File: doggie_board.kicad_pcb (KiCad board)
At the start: 4 copper layers, 117.6 x 127 mm, 110 parts, among them J1 Conn_01x03, J2 XT90PW-M, J3 XT90PW-M, J4 Conn_01x02, J5 Conn_01x03, J5V1 48v, J5V10 48v, J5V11 48v, J5V12 48v, J5V13 12v, J5V14 12v, J5V15 12v, J5V16 12v, J5V17 3.3v, J5V18 3.3v, J5V19 3.3v, J5V2 48v, J5V20 3.3v, J5V21 5v, J5V22 5v, J5V23 5v, J5V24 5v, J5V3 48v, J5V4 48v, J5V5 48v, J5V6 48v, J5V7 48v, J5V8 48v, J5V9 48v, J6 Conn_01x02, J7 Conn_01x03, J8 Conn_01x03, Q1 PSMN3R7-100BSEJ, Q10 2N7002, Q11 2N7002, Q12 2N7002, Q2 PSMN3R7-100BSEJ, Q3 PSMN3R7-100BSEJ, Q4 PSMN3R7-100BSEJ, Q5 PSMN3R7-100BSEJ, Q6 PSMN3R7-100BSEJ, Q7 Q_NMOS, Q8 Q_NMOS, Q9 2N7002, U1 TPS2490, U2 LM5148RGYR, U3 TPS566242DRLR, U4 TPS566242DRLR

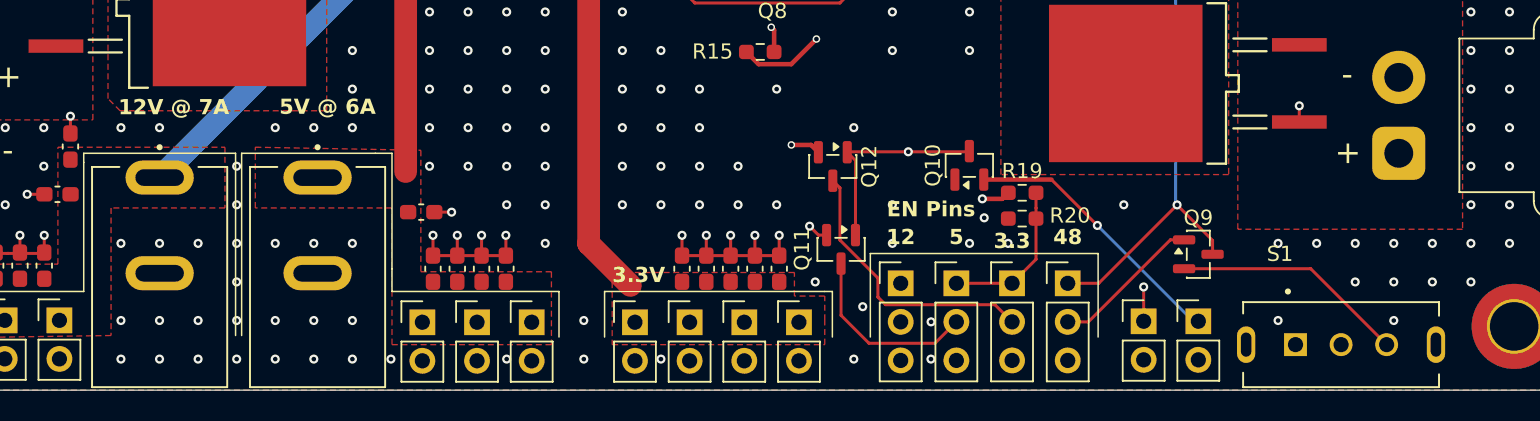
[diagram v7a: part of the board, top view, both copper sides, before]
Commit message: added header labels
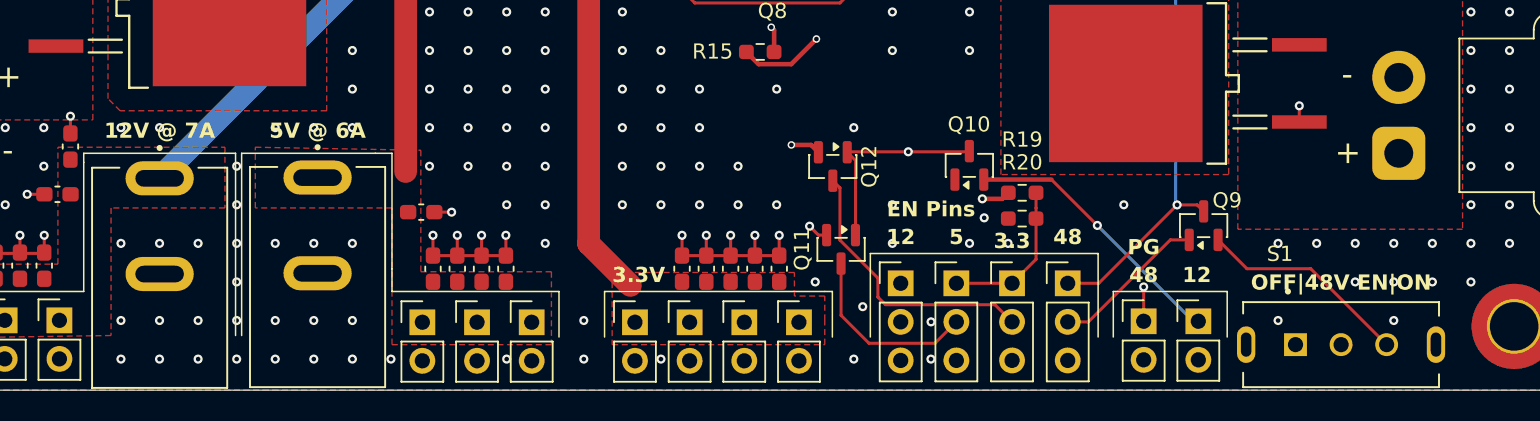
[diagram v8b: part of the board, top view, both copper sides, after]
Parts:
- moved Q9 1.92 mm to (132.6, 154.8), turned to 90 degrees
- moved J5V13 0.05 mm to (63.8, 151.7)
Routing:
- net /High Side Power Switch/sw_low: track 98.7 -> 96.4 mm
- net Net-(Q9-S): track 15.4 -> 14.0 mm
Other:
- board text added: "OFF|48V EN|ON"
- board text added: "PG"
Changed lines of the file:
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@@
 		(tags "resistor handsolder")
 		(property "Reference" "R20"
-			(at -3.15 0.2 180)
+			(at 0 3.7 180)
 			(layer "F.SilkS")
 			(effects
@@
 		(placed yes)
 		(layer "F.Cu")
-		(at 132.2 156.65)
+		(at 132.55 154.7625 90)
 		(descr "SOT, 3 Pin (JEDEC TO-236 Var AB https://www.jedec.org/document_search?search_api_views_fulltext=TO-236), generated with kicad-footprint-generator ipc_gullwing_generator.py")
 		(tags "SOT TO_SOT_SMD")
 		(property "Reference" "Q9"
-			(at 0 -2.4 0)
+			(at 1.6625 1.55 0)
 			(layer "F.SilkS")
 			(effects
@@
 		)
 		(property "Value" "2N7002"
-			(at 0 2.4 0)
+			(at 0 2.4 90)
 			(layer "F.Fab")
 			(effects
@@
 		)
 		(property "Datasheet" "https://www.onsemi.com/pub/Collateral/NDS7002A-D.PDF"
-			(at 0 0 0)
+			(at 0 0 90)
 			(layer "F.Fab")
 			(hide yes)
@@
 		)
 		(property "Description" "0.115A Id, 60V Vds, N-Channel MOSFET, SOT-23"
-			(at 0 0 0)
+			(at 0 0 90)
 			(layer "F.Fab")
 			(hide yes)
@@
 		(attr smd)
 		(fp_line
-			(start -0.76 -1.56)
-			(end 0.76 -1.56)
+			(start 0.76 -1.56)
+			(end 0.76 -0.56)
 			(stroke
 				(width 0.12)
@@
 		)
 		(fp_line
-			(start -0.76 -1.51)
-			(end -0.76 -1.56)
+			(start -0.76 -1.56)
+			(end 0.76 -1.56)
 			(stroke
 				(width 0.12)
@@
 		)
 		(fp_line
-			(start -0.76 0.39)
-			(end -0.76 -0.39)
+			(start -0.76 -1.51)
+			(end -0.76 -1.56)
 			(stroke
 				(width 0.12)
@@
 		)
 		(fp_line
-			(start -0.76 1.56)
-			(end -0.76 1.51)
+			(start -0.76 0.39)
+			(end -0.76 -0.39)
 			(stroke
 				(width 0.12)
@@
 		)
 		(fp_line
-			(start 0.76 -1.56)
-			(end 0.76 -0.56)
+			(start 0.76 0.56)
+			(end 0.76 1.56)
 			(stroke
 				(width 0.12)
@@
 		)
 		(fp_line
-			(start 0.76 0.56)
-			(end 0.76 1.56)
+			(start 0.76 1.56)
+			(end -0.76 1.56)
 			(stroke
 				(width 0.12)
@@
 		)
 		(fp_line
-			(start 0.76 1.56)
-			(end -0.76 1.56)
+			(start -0.76 1.56)
+			(end -0.76 1.51)
 			(stroke
 				(width 0.12)
@@
 		)
 		(fp_line
-			(start -1.93 -1.5)
-			(end -0.9 -1.5)
+			(start 0.9 -1.7)
+			(end 0.9 -0.55)
 			(stroke
 				(width 0.05)
@@
 		)
 		(fp_line
-			(start -1.93 -0.39)
-			(end -1.93 -1.5)
+			(start -0.9 -1.7)
+			(end 0.9 -1.7)
 			(stroke
 				(width 0.05)
@@
 		)
 		(fp_line
-			(start -1.93 0.39)
-			(end -0.9 0.39)
+			(start -0.9 -1.5)
+			(end -0.9 -1.7)
 			(stroke
 				(width 0.05)
@@
 		)
 		(fp_line
-			(start -1.93 1.5)
-			(end -1.93 0.39)
+			(start -1.93 -1.5)
+			(end -0.9 -1.5)
 			(stroke
 				(width 0.05)
@@
 		)
 		(fp_line
-			(start -0.9 -1.7)
-			(end 0.9 -1.7)
+			(start 1.93 -0.55)
+			(end 1.93 0.55)
 			(stroke
 				(width 0.05)
@@
 		)
 		(fp_line
-			(start -0.9 -1.5)
-			(end -0.9 -1.7)
+			(start 0.9 -0.55)
+			(end 1.93 -0.55)
 			(stroke
 				(width 0.05)
@@
 		)
 		(fp_line
-			(start -0.9 0.39)
-			(end -0.9 -0.39)
+			(start -1.93 -0.39)
+			(end -1.93 -1.5)
 			(stroke
 				(width 0.05)
@@
 		)
 		(fp_line
-			(start -0.9 1.5)
-			(end -1.93 1.5)
+			(start -0.9 0.39)
+			(end -0.9 -0.39)
 			(stroke
 				(width 0.05)
@@
 		)
 		(fp_line
-			(start -0.9 1.7)
-			(end -0.9 1.5)
+			(start -1.93 0.39)
+			(end -0.9 0.39)
 			(stroke
 				(width 0.05)
@@
 		)
 		(fp_line
-			(start 0.9 -1.7)
-			(end 0.9 -0.55)
+			(start 1.93 0.55)
+			(end 0.9 0.55)
 			(stroke
 				(width 0.05)
@@
 		)
 		(fp_line
-			(start 0.9 -0.55)
-			(end 1.93 -0.55)
+			(start 0.9 0.55)
+			(end 0.9 1.7)
 			(stroke
 				(width 0.05)
@@
 		)
 		(fp_line
-			(start 0.9 0.55)
-			(end 0.9 1.7)
+			(start -0.9 1.5)
+			(end -1.93 1.5)
 			(stroke
 				(width 0.05)
@@
 		)
 		(fp_line
-			(start 0.9 1.7)
-			(end -0.9 1.7)
+			(start -1.93 1.5)
+			(end -1.93 0.39)
 			(stroke
 				(width 0.05)
@@
 		)
 		(fp_line
-			(start 1.93 -0.55)
-			(end 1.93 0.55)
+			(start 0.9 1.7)
+			(end -0.9 1.7)
 			(stroke
 				(width 0.05)
@@
 		)
 		(fp_line
-			(start 1.93 0.55)
-			(end 0.9 0.55)
+			(start -0.9 1.7)
+			(end -0.9 1.5)
 			(stroke
 				(width 0.05)
@@
 		)
 		(fp_text user "${REFERENCE}"
-			(at 0 0 90)
+			(at 0 0 0)
 			(layer "F.Fab")
 			(effects
@@
 		)
 		(pad "1" smd roundrect
-			(at -0.9375 -0.95)
+			(at -0.9375 -0.95 90)
 			(size 1.475 0.6)
 			(layers "F.Cu" "F.Mask" "F.Paste")
@@
 		)
 		(pad "2" smd roundrect
-			(at -0.9375 0.95)
+			(at -0.9375 0.95 90)
 			(size 1.475 0.6)
 			(layers "F.Cu" "F.Mask" "F.Paste")
@@
 		)
 		(pad "3" smd roundrect
-			(at 0.9375 0)
+			(at 0.9375 0 90)
 			(size 1.475 0.6)
 			(layers "F.Cu" "F.Mask" "F.Paste")
@@
 		(tags "resistor handsolder")
 		(property "Reference" "R19"
-			(at 0 -1.43 0)
+			(at 0 -3.5 0)
 			(layer "F.SilkS")
 			(effects
@@
 	(footprint "footprints:CUI_PJ-037A"
 		(layer "F.Cu")
-		(at 63.8 151.6 -90)
+		(at 63.8 151.65 -90)
 		(property "Reference" "J5V13"
 			(at 2.485784 -6.76712 90)
@@
 		(tags "SOT TO_SOT_SMD")
 		(property "Reference" "Q10"
-			(at 0 -2.4 90)
+			(at 2.6941 -0.0208 0)
 			(layer "F.SilkS")
 			(effects
@@
 	)
 	(gr_line
+		(start 126.6 162.1)
+		(end 126.6 159.1)
+		(stroke
+			(width 0.1)
+			(type default)
+		)
+		(layer "F.SilkS")
+	)
+	(gr_line
 		(start 58.8 150)
 		(end 68.8 150)
@@
 	)
 	(gr_line
+		(start 134.1 159.1)
+		(end 134.1 162.1)
+		(stroke
+			(width 0.1)
+			(type default)
+		)
+		(layer "F.SilkS")
+	)
+	(gr_line
 		(start 74.3 50.2)
 		(end 74.2 54.6)
@@
 	)
 	(gr_line
+		(start 126.6 159.1)
+		(end 134.1 159.1)
+		(stroke
+			(width 0.1)
+			(type default)
+		)
+		(layer "F.SilkS")
+	)
+	(gr_line
 		(start 78 150)
 		(end 79.1 150)
@@
 		(layer "Edge.Cuts")
 	)
-	(gr_text "12V @ 7A\n"
-		(at 61.075 147.55 0)
+	(gr_text "12V @ 7A \n"
+		(at 63.8 149.1 0)
 		(layer "F.SilkS")
 		(effects
@@
 				(bold yes)
 			)
-			(justify left bottom)
+			(justify bottom)
 		)
 	)
@@
 	)
 	(gr_text "5V @ 6A"
-		(at 71.675 147.525 0)
+		(at 74.2 149.1 0)
 		(layer "F.SilkS")
 		(effects
@@
 				(bold yes)
 			)
-			(justify left bottom)
+			(justify bottom)
+		)
+	)
+	(gr_text "PG\n"
+		(at 128.6 155.6 0)
+		(layer "F.SilkS")
+		(effects
+			(font
+				(size 1 1)
+				(thickness 0.2)
+				(bold yes)
+			)
+			(justify top)
+		)
+	)
+	(gr_text "12"
+		(at 132.1 158.6 0)
+		(layer "F.SilkS")
+		(effects
+			(font
+				(size 1 1)
+				(thickness 0.2)
+				(bold yes)
+			)
+			(justify bottom)
 		)
 	)
@@
 		)
 	)
+	(gr_text "OFF|48V EN|ON"
+		(at 141.6 159.1 0)
+		(layer "F.SilkS")
+		(effects
+			(font
+				(size 1 1)
+				(thickness 0.2)
+				(bold yes)
+			)
+			(justify bottom)
+		)
+	)
 	(gr_text "Made by: Niranjan Mathirajan, Siddharth Vasudevan, Alperen Ozpolat"
 		(at 65.2 43.8 0)
@@
 		)
 	)
+	(gr_text "48"
+		(at 128.6 158.6 0)
+		(layer "F.SilkS")
+		(effects
+			(font
+				(size 1 1)
+				(thickness 0.2)
+				(bold yes)
+			)
+			(justify bottom)
+		)
+	)
 	(gr_text "12"
 		(at 112.6 156.1 0)
@@
 	)
 	(segment
-		(start 133.1375 155.7375)
-		(end 130.8 153.4)
+		(start 130.8 153.4)
+		(end 132.125 153.4)
 		(width 0.2)
 		(layer "F.Cu")
@@
 	)
 	(segment
-		(start 133.1375 156.65)
-		(end 133.1375 155.7375)
+		(start 132.125 153.4)
+		(end 132.55 153.825)
 		(width 0.2)
 		(layer "F.Cu")
@@
 	)
 	(segment
-		(start 131.2625 157.6)
+		(start 133.5 155.7)
+		(end 135.4 157.6)
+		(width 0.2)
+		(layer "F.Cu")
+		(net 34)
+	)
+	(segment
+		(start 135.4 157.6)
 		(end 139.6 157.6)
 		(width 0.2)
